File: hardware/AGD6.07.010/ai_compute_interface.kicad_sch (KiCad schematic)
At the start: 19 parts, among them J601 AI_SIGNALS GH8, J602 AI_OFF_SWITCH GH2, J603 SERVICE USB-C, J604 AI_USB GH4, U602 TPD4E05U06DQA, U603 USBLC6-2SC6

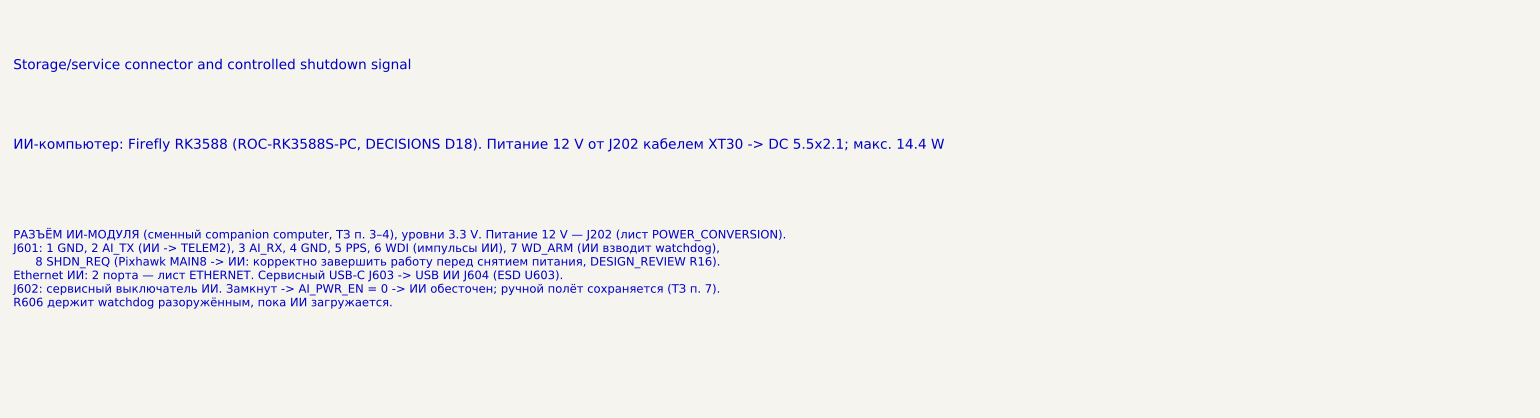
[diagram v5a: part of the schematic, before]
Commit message: AGD6.07.010 rev 0.4 (WIP): 3x TRACO THL40 DC/DC, split 12 V bus, SwitchBlox Ethernet, fixed LM5069 UVLO/OVLO, computed hot-swap values, PX4 firmware notes; board re-placed, routing in progress
Co-Authored-By: Claude Opus 5.5 <noreply@anthropic.com>
Claude-Session: https://claude.ai/code/session_01Qk7uTKdi6YbndB9fGuguYV
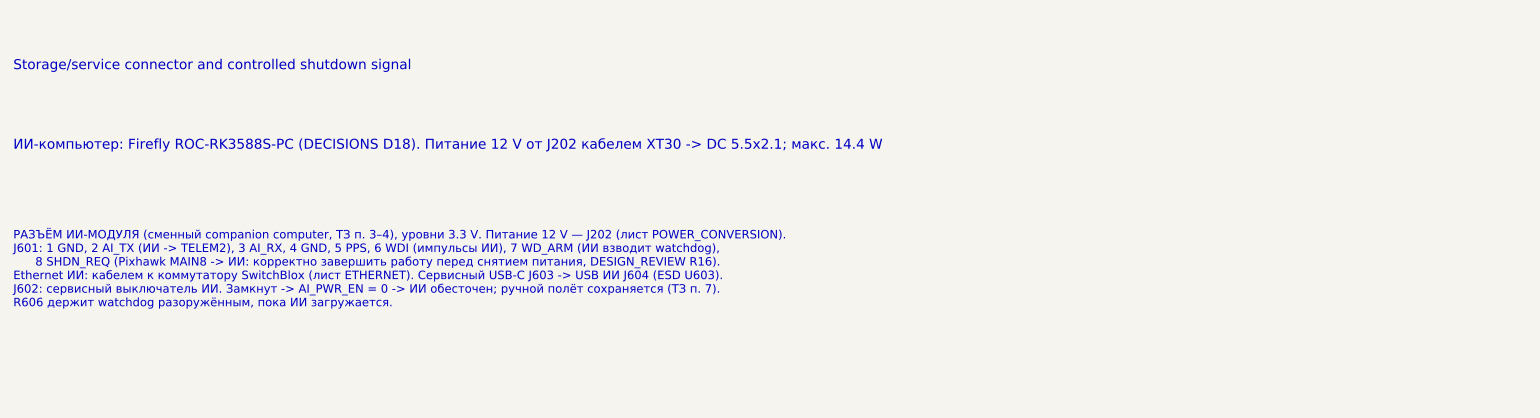
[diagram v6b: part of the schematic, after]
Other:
- note added: "ИИ-компьютер: Firefly ROC-RK3588S-PC (DECISIONS D18). Питание 12 V от J202 кабелем XT30 -> DC 5.5x2.1; макс. 14.4 W"
- note added: "РАЗЪЁМ ИИ-МОДУЛЯ (сменный companion computer, ТЗ п. 3–4), уровни 3.3 V. Питание 12 V — J202 (лист POWER_CONVERSION). J601: 1 GND, 2 AI_TX (ИИ -> TELEM2), 3 AI_RX, 4 GND, 5 PPS, 6 WDI (импульсы ИИ), 7 WD_ARM (ИИ взводит watchdog), 8 SHDN_REQ (Pixhawk MAIN8 -> ИИ: корректно завершить работу перед снятием питания, DESIGN_REVIEW R16). Ethernet ИИ: кабелем к коммутатору SwitchBlox (лист ETHERNET). Сер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"
- note removed: "ИИ-компьютер: Firefly RK3588 (ROC-RK3588S-PC, DECISIONS D18). Питание 12 V от J202 кабелем XT30 -> DC 5.5x2.1; макс. 14.4 W"
- note removed: "РАЗЪЁМ ИИ-МОДУЛЯ (сменный companion computer, ТЗ п. 3–4), уровни 3.3 V. Питание 12 V — J202 (лист POWER_CONVERSION). J601: 1 GND, 2 AI_TX (ИИ -> TELEM2), 3 AI_RX, 4 GND, 5 PPS, 6 WDI (импульсы ИИ), 7 WD_ARM (ИИ взводит watchdog), 8 SHDN_REQ (Pixhawk MAIN8 -> ИИ: корректно завершить работу перед снятием питания, DESIGN_REVIEW R16). Ethernet ИИ: 2 порта — лист ETHERNET. Сервисный USB-C J603 -> USB 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"
